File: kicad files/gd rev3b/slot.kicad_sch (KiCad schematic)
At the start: 25 parts, among them J10 Apple_II_Slot, J9 IO-Xtra, SW2 DEV, SW3 IOSEL, U12 Slotmaker, U13 74HC245, U32 LM7905_TO220

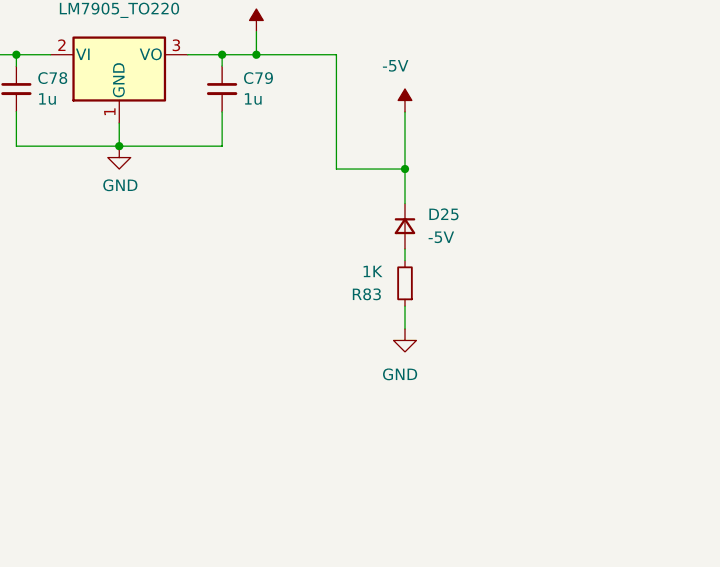
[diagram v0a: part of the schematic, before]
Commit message: Schematic changes for #52, #50, #70, #51, #61, #69, #71
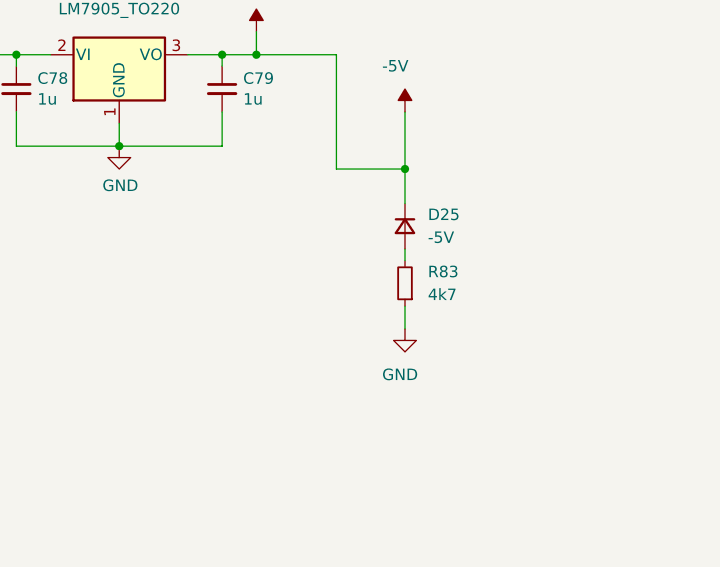
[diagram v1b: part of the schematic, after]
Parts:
- R83: value 1K -> 4k7
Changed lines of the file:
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@@
   (symbol (lib_id "Mega IIe Rev3 Symbols:R_0805") (at 238.76 139.7 180) (unit 1)
     (in_bom yes) (on_board yes) (dnp no) (fields_autoplaced)
-    (property "Reference" "R83" (at 236.22 140.9701 0)
-      (effects (font (size 1.27 1.27)) (justify left))
+    (property "Reference" "R83" (at 241.3 138.43 0)
+      (effects (font (size 1.27 1.27)) (justify right))
     )
-    (property "Value" "1K" (at 236.22 138.4301 0)
-      (effects (font (size 1.27 1.27)) (justify left))
+    (property "Value" "4k7" (at 241.3 140.97 0)
+      (effects (font (size 1.27 1.27)) (justify right))
     )
     (property "Footprint" "Resistor_SMD:R_0805_2012Metric" (at 238.76 139.7 0)
